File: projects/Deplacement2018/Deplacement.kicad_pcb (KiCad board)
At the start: 2 copper layers, 67.3 x 80 mm, 15 parts, among them J1 alim_logique_5V, J2 moteur_droit, J3 moteur_gauche, J4 Conn_01x03, J5 QEI_droite, J6 QEI_gauche, U1 black_pill

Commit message: maj HE14
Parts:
- J1, J4: footprint robot:HE13-3 -> robot:HE14-3_horizontal
- J5, J6: footprint Connector_Molex:Molex_KK-254_AE-6410-05A_1x05_P2.54mm_Vertical -> robot:HE14-5_horizontal
- moved J5 13.7 mm to (148.6, 94.0), turned to 270 degrees
- moved J6 12.5 mm to (148.6, 78.7), turned to 270 degrees
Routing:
- net +5V: track 67.2 -> 92.2 mm
- net QEI_droite_1: track 17.8 -> 31.2 mm
- net QEI_gauche_1: track 97.0 -> 110.0 mm
- net QEI_gauche_2: track 102.2 -> 106.6 mm
- net QEI_droite_2: track 17.8 -> 19.1 mm
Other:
- board text added: "QEI"
- board text removed: "QEI -> G"

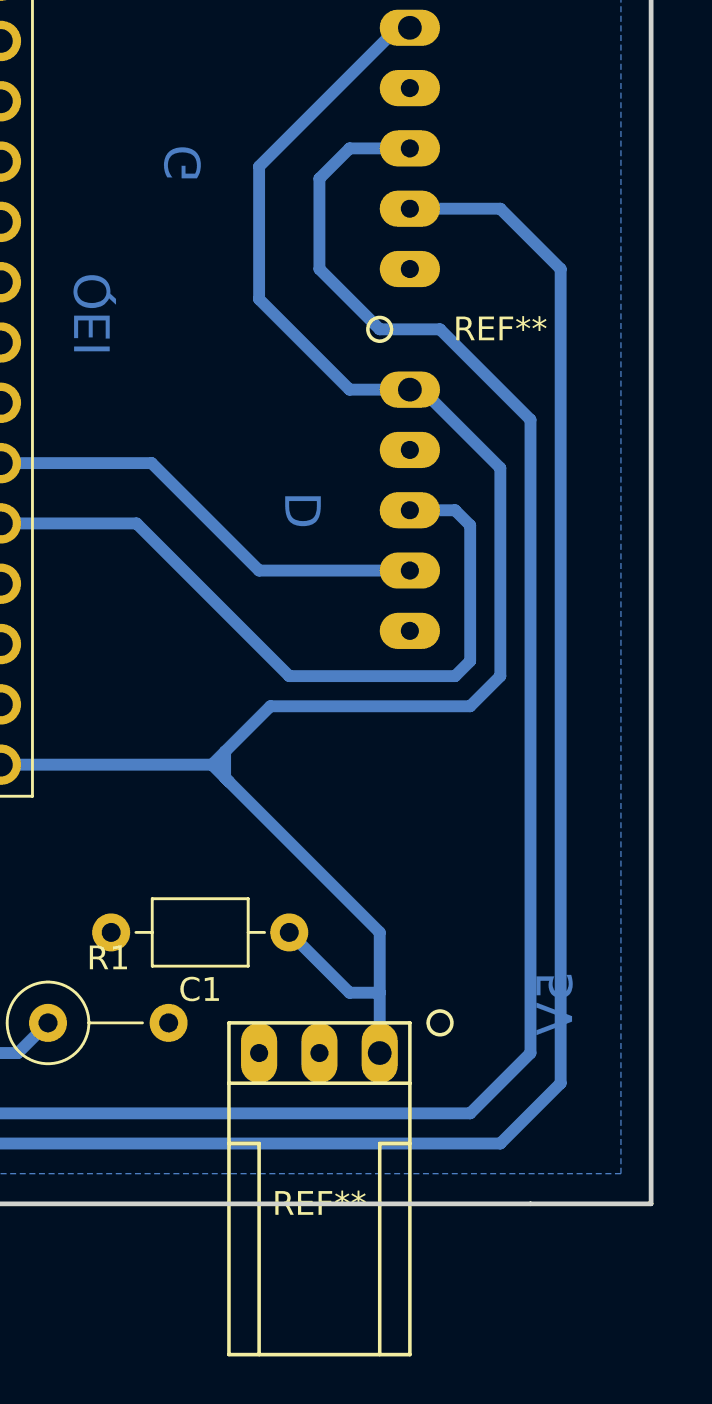
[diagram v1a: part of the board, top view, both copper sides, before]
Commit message: Fixed QEI inversion.
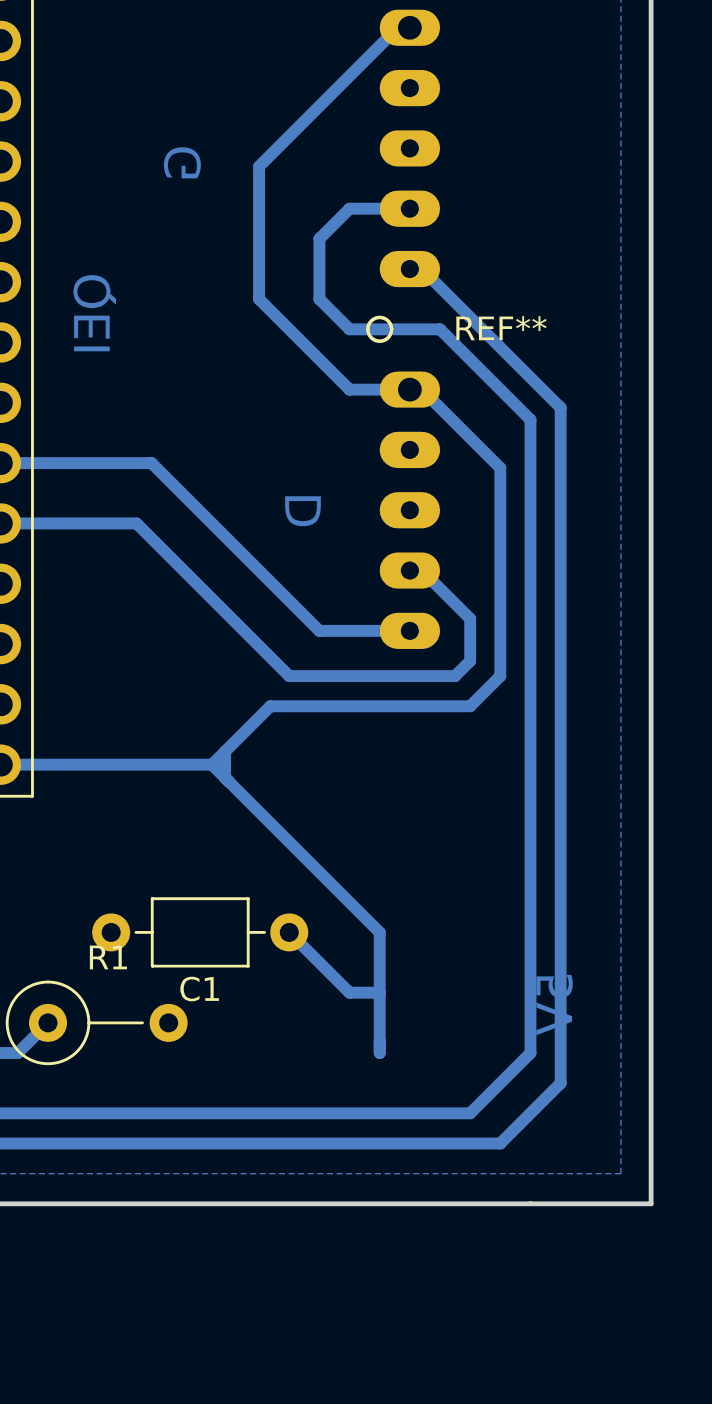
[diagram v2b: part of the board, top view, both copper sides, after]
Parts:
- removed J1: alim_logique_5V, robot:HE14-3_horizontal
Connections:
- J5 pad 3: QEI_droite_1 -> Net-(J5-Pad3)
- J5 pad 4: QEI_droite_2 -> QEI_droite_1
- J5 pad 5: Net-(J5-Pad5) -> QEI_droite_2
- J6 pad 3: QEI_gauche_1 -> Net-(J6-Pad3)
- J6 pad 4: QEI_gauche_2 -> QEI_gauche_1
- J6 pad 5: Net-(J6-Pad5) -> QEI_gauche_2
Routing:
- net QEI_gauche_2: track 106.6 -> 101.6 mm
- net QEI_droite_1: track 31.2 -> 27.9 mm
- net QEI_gauche_1: track 110.0 -> 108.7 mm
- net QEI_droite_2: track 19.1 -> 20.2 mm

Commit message: maj pcb
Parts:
- added J1: alim_logique_5V, robot:HE14-3_horizontal, F.Cu at (141.0, 123.2)
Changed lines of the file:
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@@
-(kicad_pcb (version 20171130) (host pcbnew "(5.0.1)-3")
+(kicad_pcb (version 20171130) (host pcbnew "(5.0.1-3-g963ef8bb5)")
   (general
     (thickness 1.6)
@@
     (tracks 113)
     (zones 0)
-    (modules 14)
-    (nets 45)
+    (modules 15)
+    (nets 46)
   )
   (page A4)
@@
   (net 43 "Net-(J5-Pad3)")
   (net 44 "Net-(J6-Pad3)")
+  (net 45 "Net-(J1-Pad3)")
   (net_class Default "This is the default net class."
     (clearance 0.2)
@@
     (add_net "Net-(D1-Pad1)")
     (add_net "Net-(D2-Pad1)")
+    (add_net "Net-(J1-Pad3)")
     (add_net "Net-(J2-Pad4)")
     (add_net "Net-(J3-Pad4)")
@@
     (uvia_drill 0.1)
   )
+  (module robot:HE14-3_horizontal (layer F.Cu)
+    (at 140.97 123.19 180)
+    (tags "HE13 3 logique")
+    (fp_text reference J1 (at 0 -2.54 180) (layer F.SilkS) hide
+      (effects (font (size 1 1) (thickness 0.15)))
+    )
+    (fp_text value alim_logique_5V (at 0 1.27) (layer F.Fab) hide
+      (effects (font (size 1 1) (thickness 0.15)))
+    )
+    (fp_text user REF** (at 0 -2.54) (layer F.SilkS)
+      (effects (font (size 1 1) (thickness 0.15)))
+    )
+    (fp_line (start 3.81 2.54) (end -3.81 2.54) (layer F.Fab) (width 0.15))
+    (fp_line (start 2.54 0) (end 3.81 0) (layer F.Fab) (width 0.15))
+    (fp_line (start 2.54 -8.89) (end 2.54 0) (layer F.Fab) (width 0.15))
+    (fp_line (start -2.54 0) (end -3.81 0) (layer F.Fab) (width 0.15))
+    (fp_line (start -2.54 -8.89) (end -2.54 0) (layer F.Fab) (width 0.15))
+    (fp_line (start 3.81 -8.89) (end -3.81 -8.89) (layer F.Fab) (width 0.15))
+    (fp_line (start 3.81 5.08) (end 3.81 -8.89) (layer F.Fab) (width 0.15))
+    (fp_line (start -3.81 5.08) (end 3.81 5.08) (layer F.Fab) (width 0.15))
+    (fp_line (start -3.81 -8.89) (end -3.81 5.08) (layer F.Fab) (width 0.15))
+    (fp_circle (center -5.08 5.08) (end -4.58 5.08) (layer F.SilkS) (width 0.15))
+    (fp_line (start 3.81 2.54) (end 3.81 5.08) (layer F.SilkS) (width 0.15))
+    (fp_line (start 3.81 5.08) (end -3.81 5.08) (layer F.SilkS) (width 0.15))
+    (fp_line (start -3.81 5.08) (end -3.81 2.54) (layer F.SilkS) (width 0.15))
+    (fp_line (start -3.81 2.54) (end 3.81 2.54) (layer F.SilkS) (width 0.15))
+    (fp_line (start 3.81 -8.89) (end 3.81 2.54) (layer F.SilkS) (width 0.15))
+    (fp_line (start 3.81 -8.89) (end -3.81 -8.89) (layer F.SilkS) (width 0.15))
+    (fp_line (start -3.81 -8.89) (end -3.81 2.54) (layer F.SilkS) (width 0.15))
+    (fp_line (start -3.81 0) (end -2.54 0) (layer F.SilkS) (width 0.15))
+    (fp_line (start -2.54 0) (end -2.54 -8.89) (layer F.SilkS) (width 0.15))
+    (fp_line (start 2.54 -8.89) (end 2.54 0) (layer F.SilkS) (width 0.15))
+    (fp_line (start 2.54 0) (end 3.81 0) (layer F.SilkS) (width 0.15))
+    (pad 2 thru_hole oval (at 0 3.81 180) (size 1.524 2.54) (drill 0.762) (layers *.Cu *.Mask)
+      (net 5 GND))
+    (pad 1 thru_hole oval (at -2.54 3.81 180) (size 1.524 2.54) (drill 1) (layers *.Cu *.Mask)
+      (net 2 +5V))
+    (pad 3 thru_hole oval (at 2.54 3.81 180) (size 1.524 2.54) (drill 0.762) (layers *.Cu *.Mask)
+      (net 45 "Net-(J1-Pad3)"))
+    (model /Users/alex/Desktop/c-281698-3-g-3d.stp
+      (offset (xyz 0 9 3))
+      (scale (xyz 1 1 1))
+      (rotate (xyz -90 0 180))
+    )
+  )
   (module robot:HE14-5_horizontal (layer F.Cu)
     (at 148.59 93.98 270)
@@
     (effects (font (size 1.5 1.5) (thickness 0.3)) (justify mirror))
   )
-  (gr_text 5V (at 150.91664 117.28704 90) (layer B.Cu)
+  (gr_text 5V (at 147.32 114.3 90) (layer B.Cu)
     (effects (font (size 1.5 1.5) (thickness 0.3)) (justify mirror))
   )

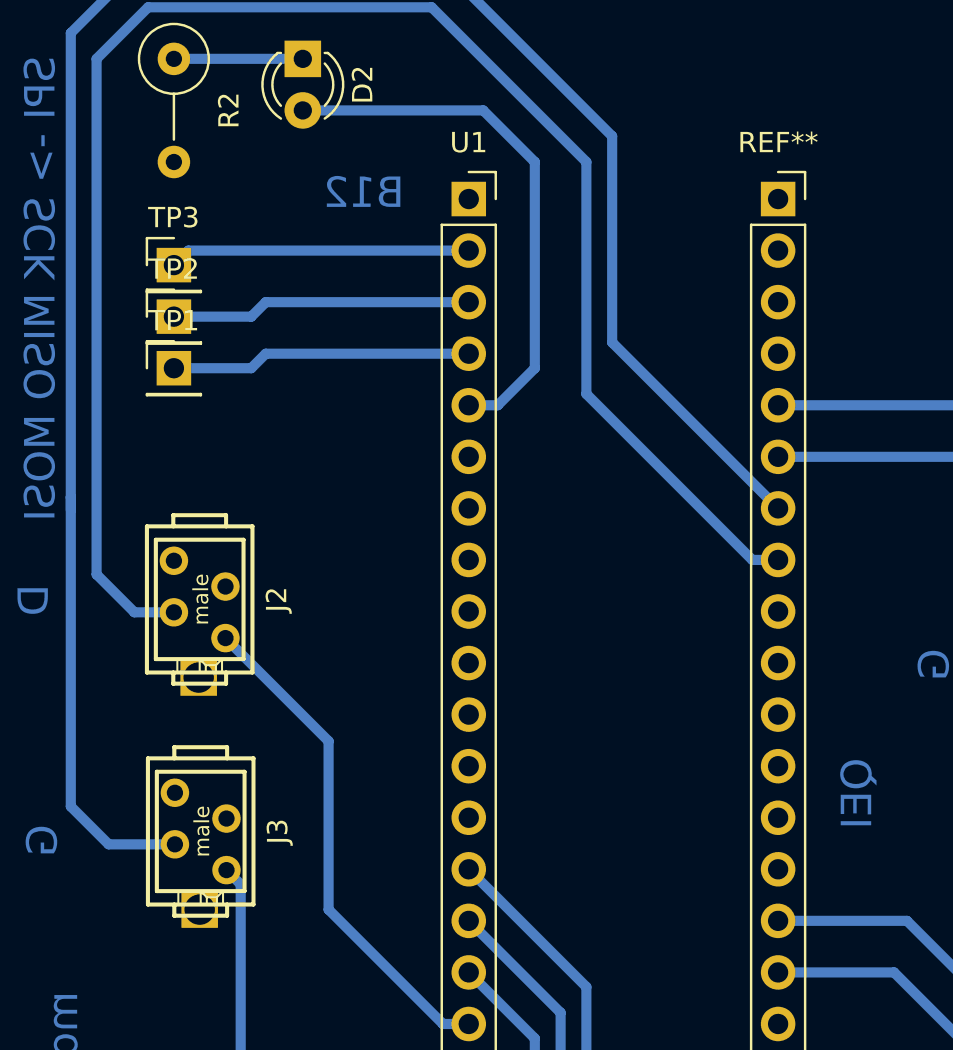
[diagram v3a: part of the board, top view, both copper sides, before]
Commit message: Better footprints for micromatch. Added a 3D model library to the club models.
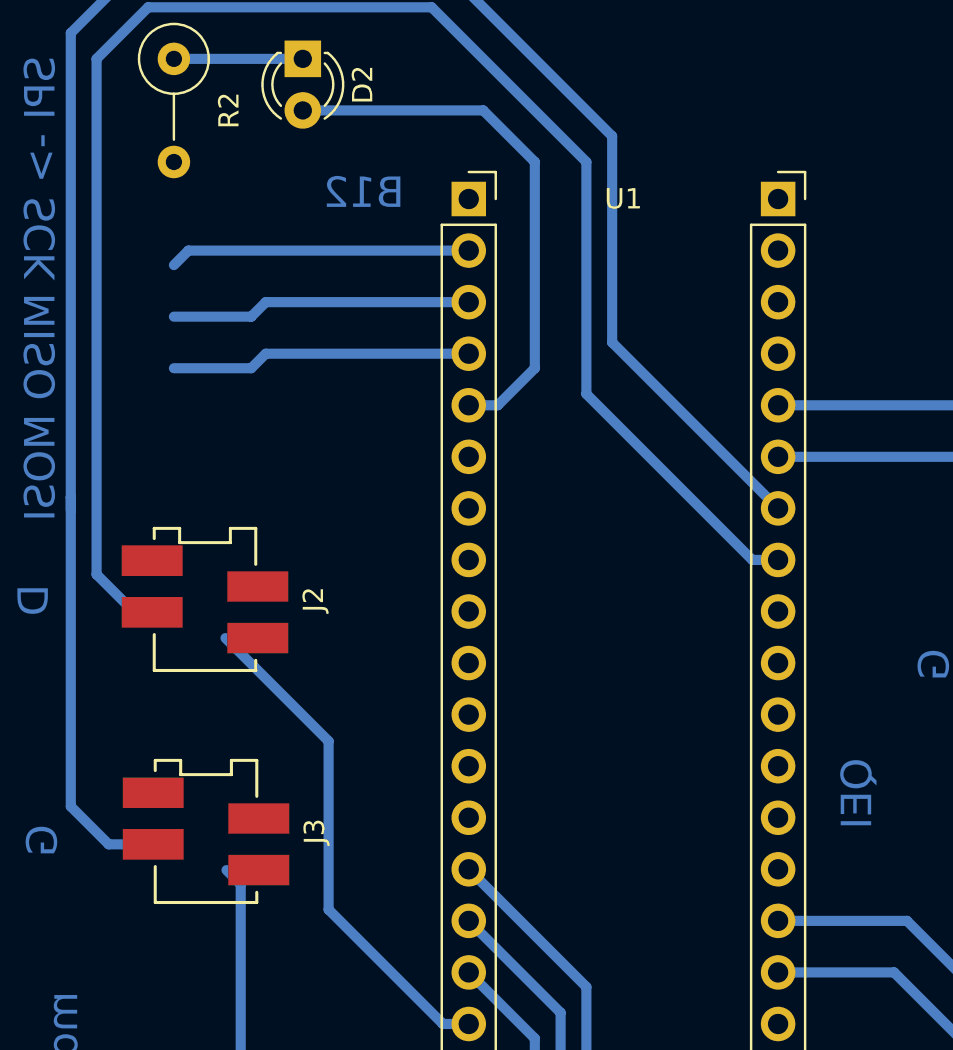
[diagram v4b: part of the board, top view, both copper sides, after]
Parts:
- removed TP1, TP2, TP3: TestPoint, Connector_PinHeader_2.54mm:PinHeader_1x01_P2.54mm_Vertical
- J1, J4: footprint robot:HE14-3_horizontal -> @Robot:HE14-3_horizontal
- J2, J3: footprint robot:micromatch-4-pin-male -> @Robot:ConnectorMicromatch-4
- J5, J6: footprint robot:HE14-5_horizontal -> @Robot:HE14-5_horizontal
- U1: footprint robot:blackpill -> @Robot:black_pill

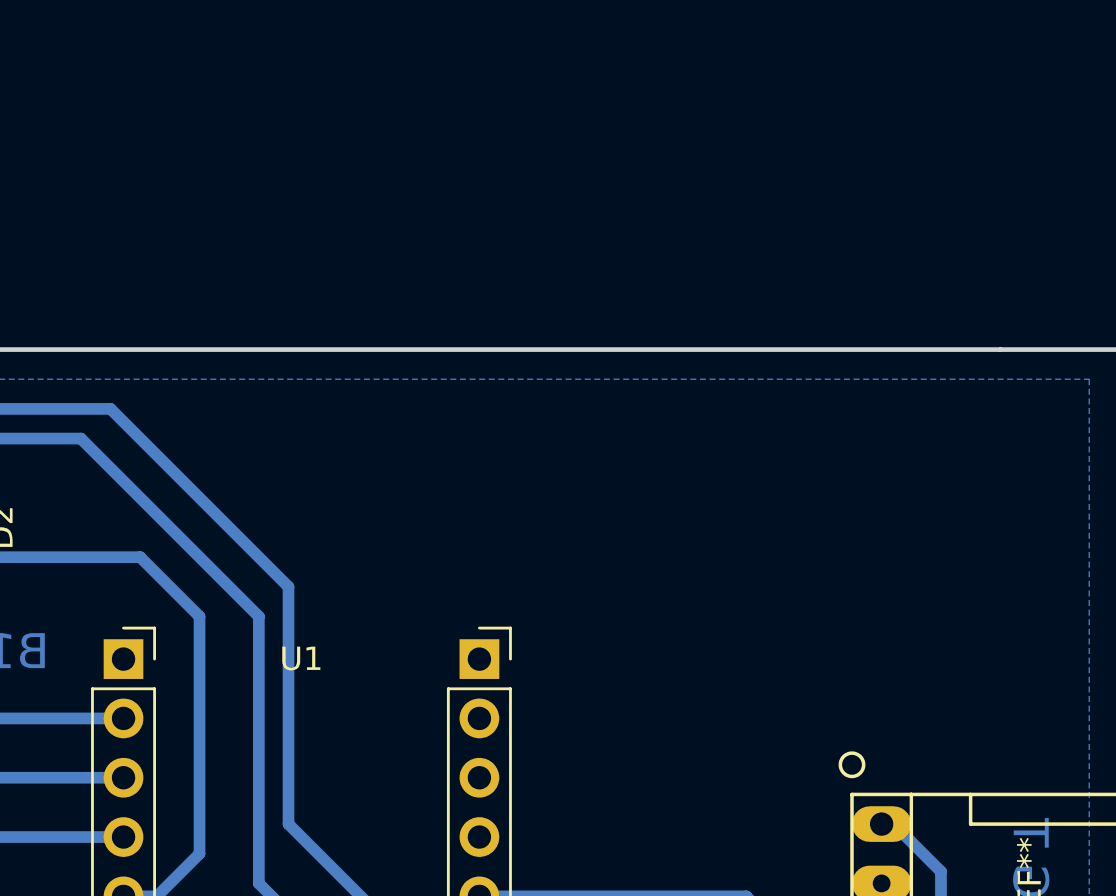
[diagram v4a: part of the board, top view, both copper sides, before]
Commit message: Created 'blocs' repo to store elementary functions to be included on future PCBs
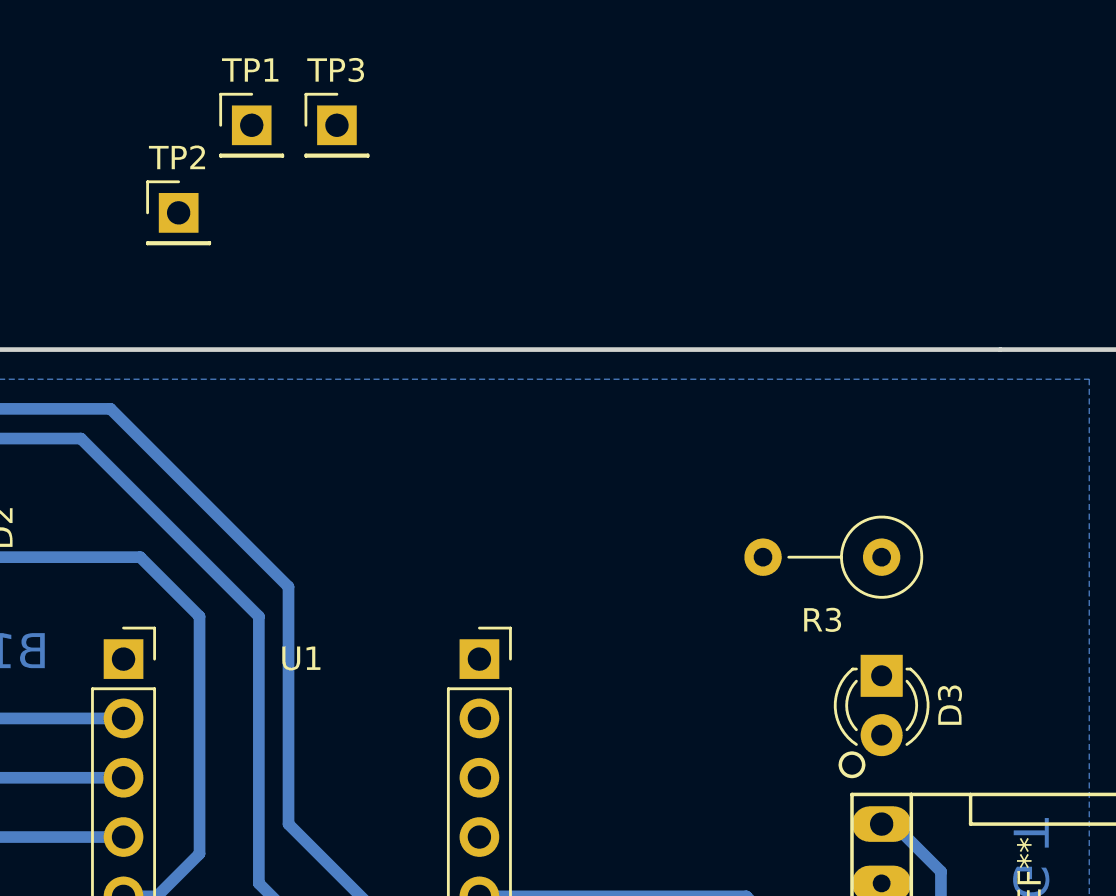
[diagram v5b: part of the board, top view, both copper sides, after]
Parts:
- added D3: LED, LED_THT:LED_D3.0mm, F.Cu at (144.8, 59.7)
- added R3: R, Resistor_THT:R_Axial_DIN0309_L9.0mm_D3.2mm_P5.08mm_Vertical, F.Cu at (144.8, 54.6)
- added TP1: TestPoint, Connector_PinHeader_2.54mm:PinHeader_1x01_P2.54mm_Vertical, F.Cu at (117.8, 36.1)
- added TP2: TestPoint, Connector_PinHeader_2.54mm:PinHeader_1x01_P2.54mm_Vertical, F.Cu at (114.7, 39.9)
- added TP3: TestPoint, Connector_PinHeader_2.54mm:PinHeader_1x01_P2.54mm_Vertical, F.Cu at (121.5, 36.1)
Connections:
- net TX renamed LED_TX
- U1 pad 18: Net-(U1-Pad18) -> +5V
- U1 pad 40: +5V -> Net-(U1-Pad40)
